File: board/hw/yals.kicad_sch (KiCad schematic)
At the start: 1 part, among them J2 UART

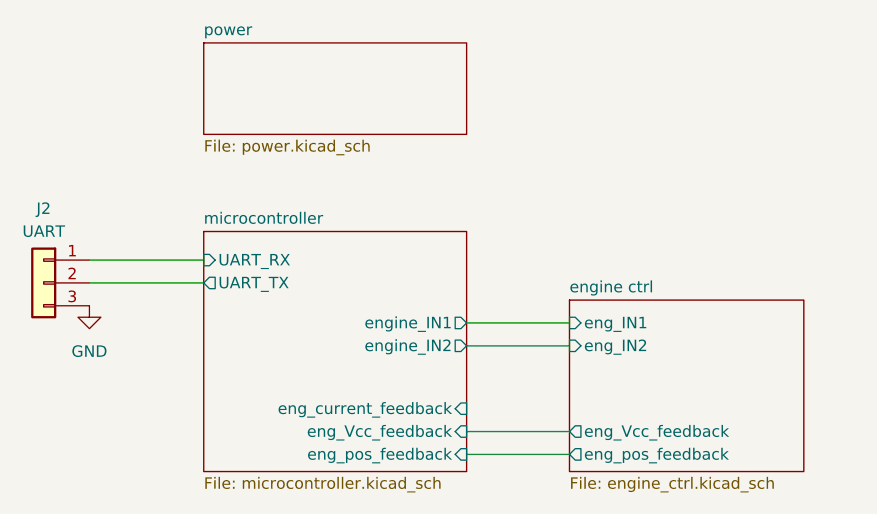
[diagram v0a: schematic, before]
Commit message: added current measuing circuit
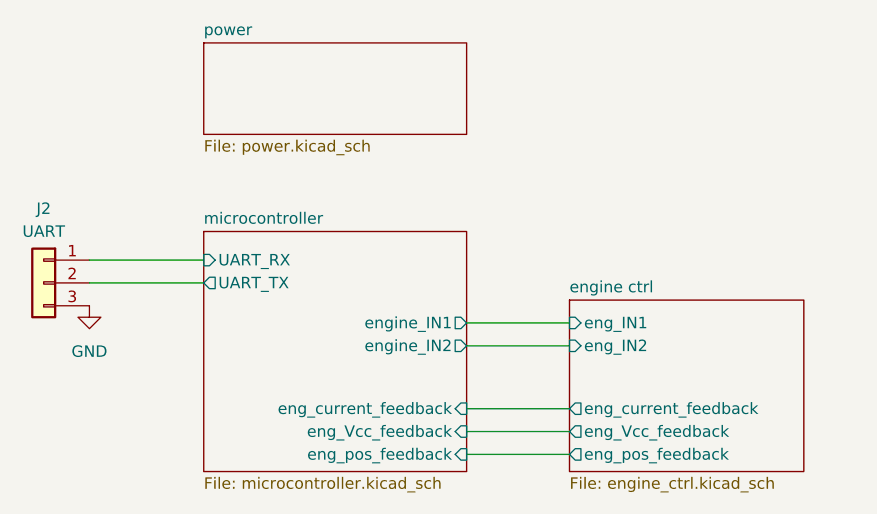
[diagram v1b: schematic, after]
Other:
- sheet engine ctrl ports: added eng_current_feedback; removed none
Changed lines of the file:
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@@
+    (stroke (width 0) (type default))
+  )
+  (wire (pts (xy 151.13 104.775) (xy 162.56 104.775))
     (stroke (width 0) (type default))
   )
@@
       (effects (font (size 1.27 1.27)) (justify left))
     )
+    (pin "eng_current_feedback" output (at 162.56 104.775 180)
+      (effects (font (size 1.27 1.27)) (justify left))
+    )
